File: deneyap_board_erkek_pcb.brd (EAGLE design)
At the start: 160 x 100 mm, 4 parts

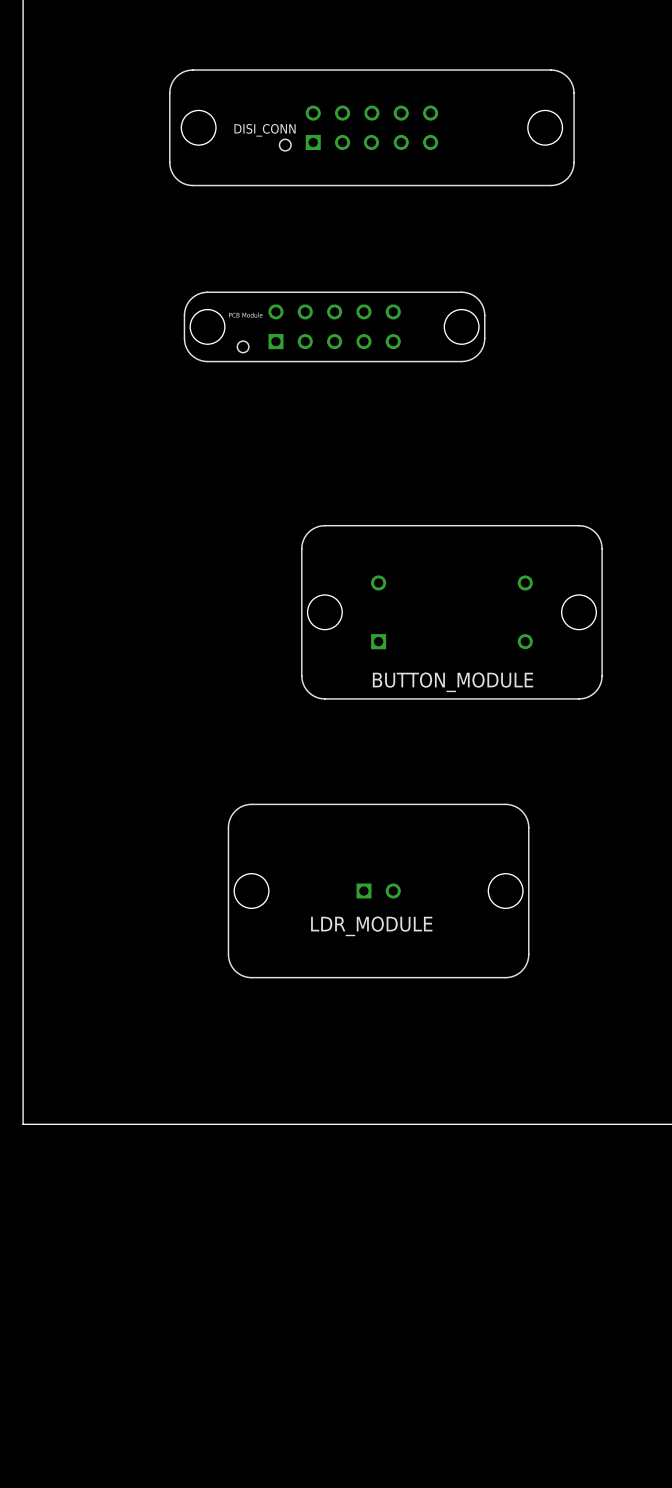
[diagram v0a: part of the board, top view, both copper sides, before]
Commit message: Update deneyap_board_erkek_pcb.brd
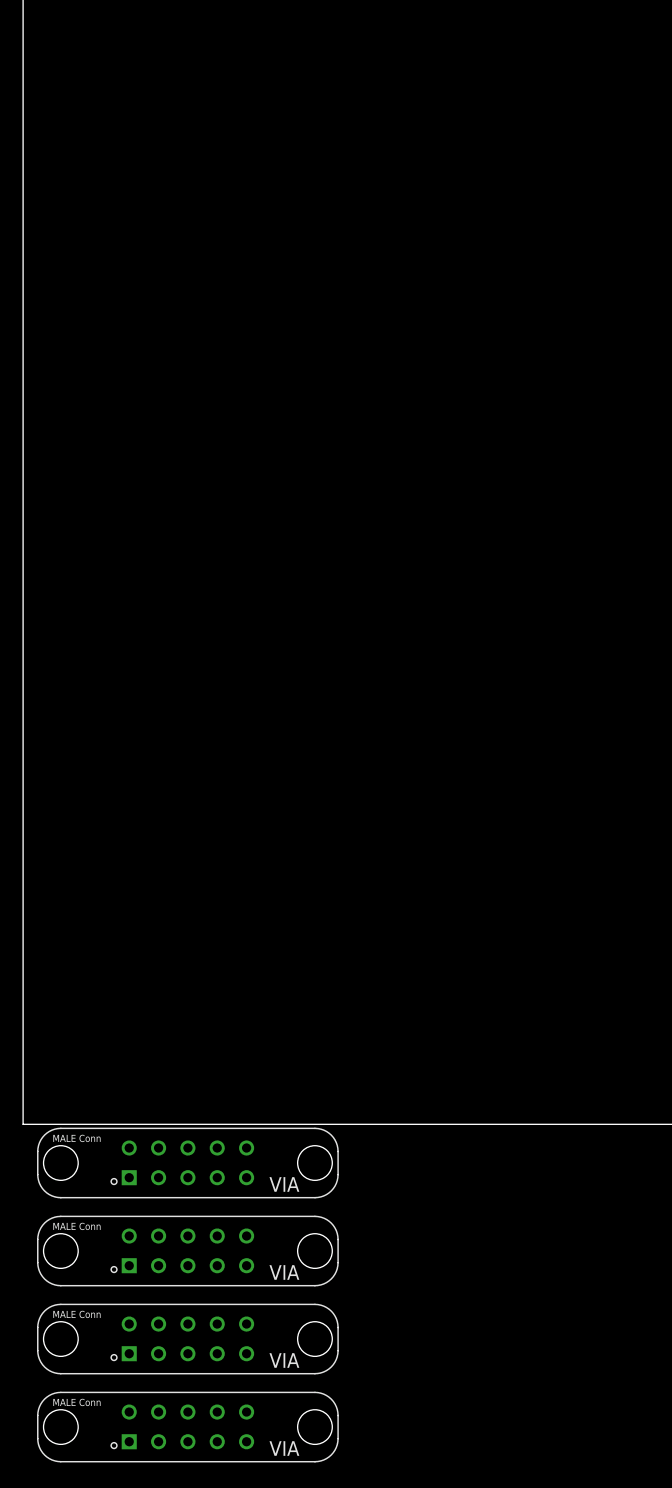
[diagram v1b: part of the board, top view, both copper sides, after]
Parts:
- U$1: value PCB_BUTTON_MODULE -> PCB_ERKEK_CONNECTORA; device deneyap_board_erkek_pcb_lib:PCB_BUTTON_MODULE -> deneyap_board_erkek_pcb_lib:PCB_ERKEK_CONNECTOR
- U$2: value PCB_DISI_CONNECTORA -> PCB_ERKEK_CONNECTORA; device deneyap_board_erkek_pcb_lib:PCB_DISI_CONNECTOR -> deneyap_board_erkek_pcb_lib:PCB_ERKEK_CONNECTOR
- U$4: value PCB_LDR_MODULE -> PCB_ERKEK_CONNECTORA; device deneyap_board_erkek_pcb_lib:PCB_LDR_MODULE -> deneyap_board_erkek_pcb_lib:PCB_ERKEK_CONNECTOR
- moved U$2 95.9 mm to (1.27, -14.0)
- moved U$3 88.5 mm to (1.27, -21.6)
- moved U$1 48.9 mm to (1.27, -6.35)
- moved U$4 45.0 mm to (1.27, -29.2)
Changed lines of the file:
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@@
 <drawing>
 <settings>
-<setting alwaysvectorfont="yes"/>
+<setting alwaysvectorfont="no"/>
 <setting verticaltext="up"/>
 </settings>
@@
 </autorouter>
 <elements>
-<element name="U$1" library="deneyap_board_erkek_pcb_lib" package="PCB_BUTTON_MODULE" value="PCB_BUTTON_MODULE" x="24.13" y="36.83" smashed="yes"/>
-<element name="U$2" library="deneyap_board_erkek_pcb_lib" package="PCB_DISI_CONNECTOR" value="PCB_DISI_CONNECTORA" x="12.7" y="81.28" smashed="yes"/>
-<element name="U$3" library="deneyap_board_erkek_pcb_lib" package="PCB_ERKEK_CONNECTOR" value="PCB_ERKEK_CONNECTORA" x="13.97" y="66.04" smashed="yes"/>
-<element name="U$4" library="deneyap_board_erkek_pcb_lib" package="PCB_LDR_MODULE" value="PCB_LDR_MODULE" x="17.78" y="12.7" smashed="yes"/>
+<element name="U$1" library="deneyap_board_erkek_pcb_lib" package="PCB_ERKEK_CONNECTOR" value="PCB_ERKEK_CONNECTORA" x="1.27" y="-6.35" smashed="yes"/>
+<element name="U$2" library="deneyap_board_erkek_pcb_lib" package="PCB_ERKEK_CONNECTOR" value="PCB_ERKEK_CONNECTORA" x="1.27" y="-13.97" smashed="yes"/>
+<element name="U$3" library="deneyap_board_erkek_pcb_lib" package="PCB_ERKEK_CONNECTOR" value="PCB_ERKEK_CONNECTORA" x="1.27" y="-21.59" smashed="yes"/>
+<element name="U$4" library="deneyap_board_erkek_pcb_lib" package="PCB_ERKEK_CONNECTOR" value="PCB_ERKEK_CONNECTORA" x="1.27" y="-29.21" smashed="yes"/>
 </elements>
 <signals>

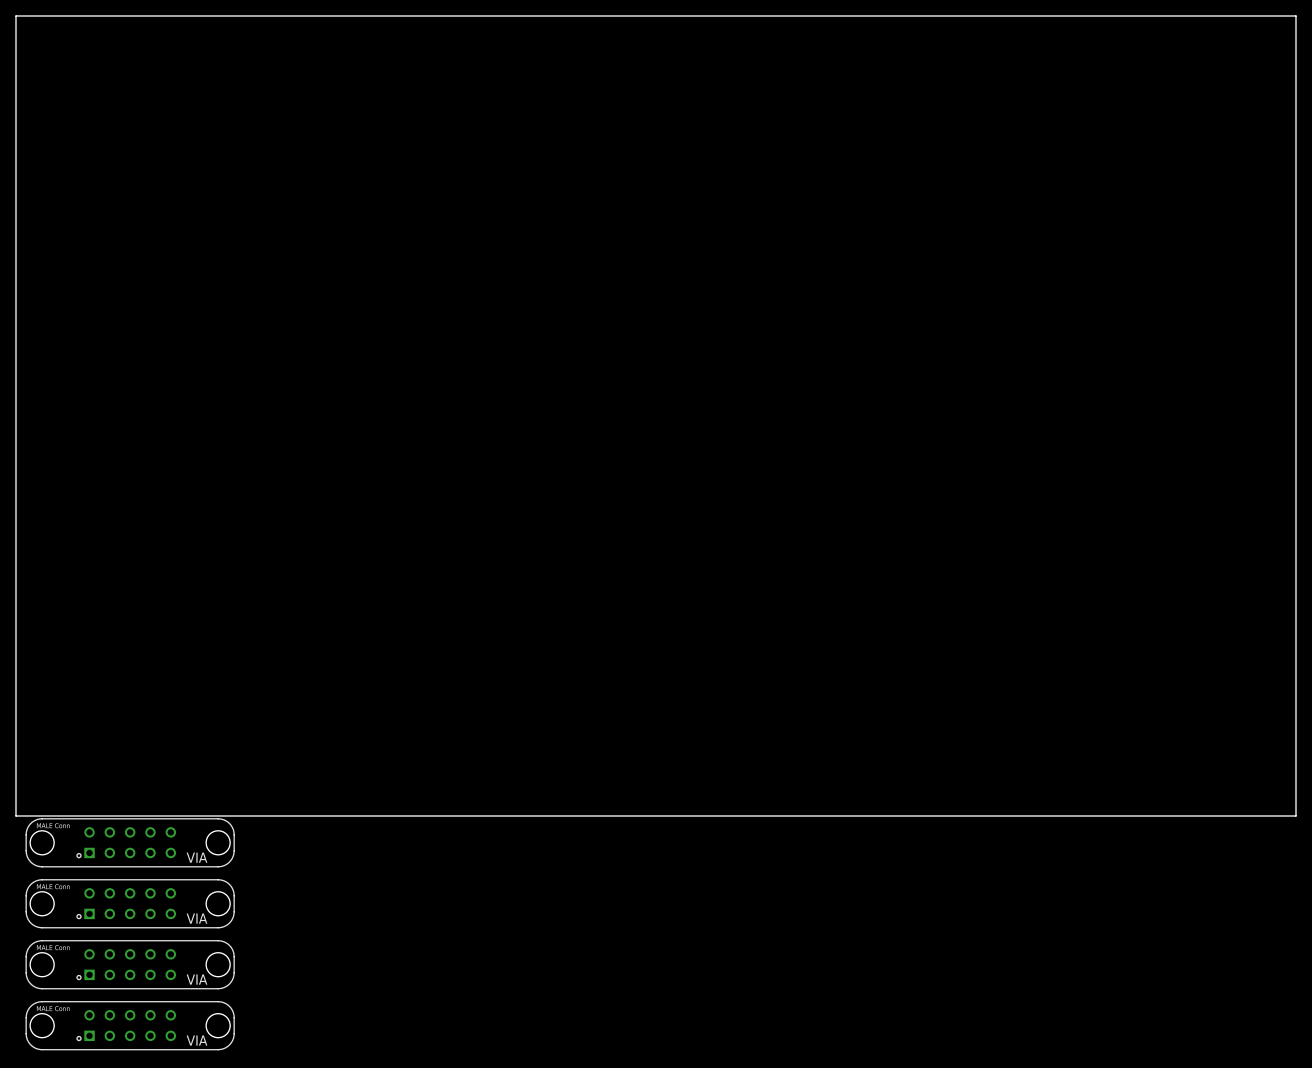
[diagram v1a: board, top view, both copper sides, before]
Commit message: Update deneyap_board_erkek_pcb.brd
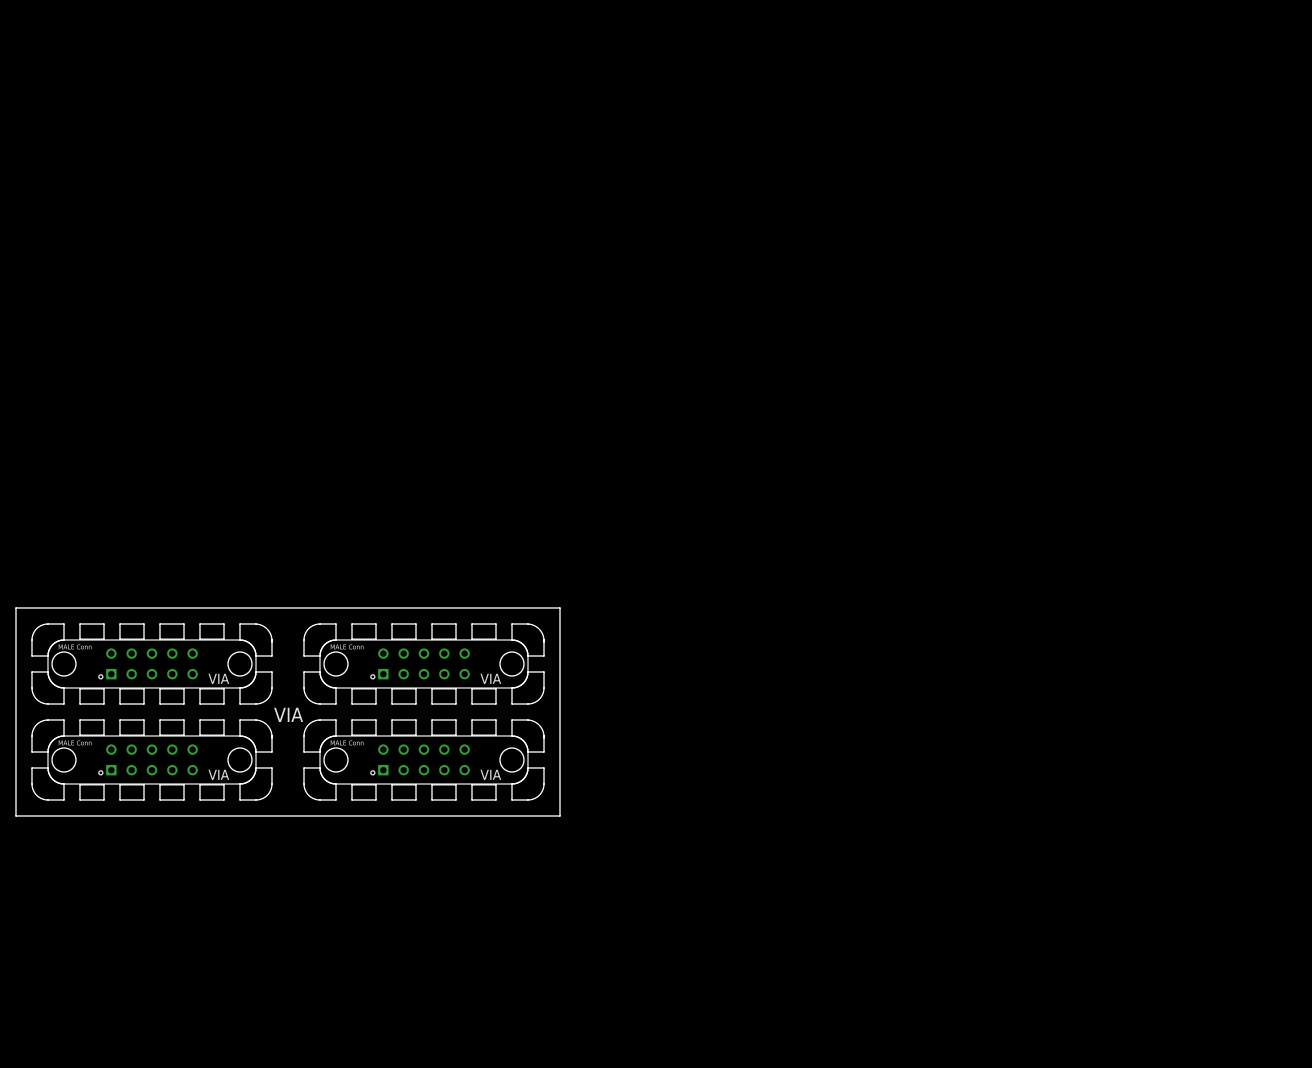
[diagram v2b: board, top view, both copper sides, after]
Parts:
- moved U$4 49.5 mm to (38.0, 4.00)
- moved U$2 47.4 mm to (38.0, 16.0)
- moved U$3 25.7 mm to (4.00, 4.00)
- moved U$1 22.5 mm to (4.00, 16.0)
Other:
- board size 160 x 100 mm -> 68 x 26 mm
- board text added: "VIA"
